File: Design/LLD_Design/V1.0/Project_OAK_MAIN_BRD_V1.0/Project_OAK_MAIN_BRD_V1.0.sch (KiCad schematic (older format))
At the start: 104 parts, among them U1 ATmega328PB-MU, U2 RV-8263-C7-32.768KHZ-20PPM-TA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, U3 LIS2DW12TR

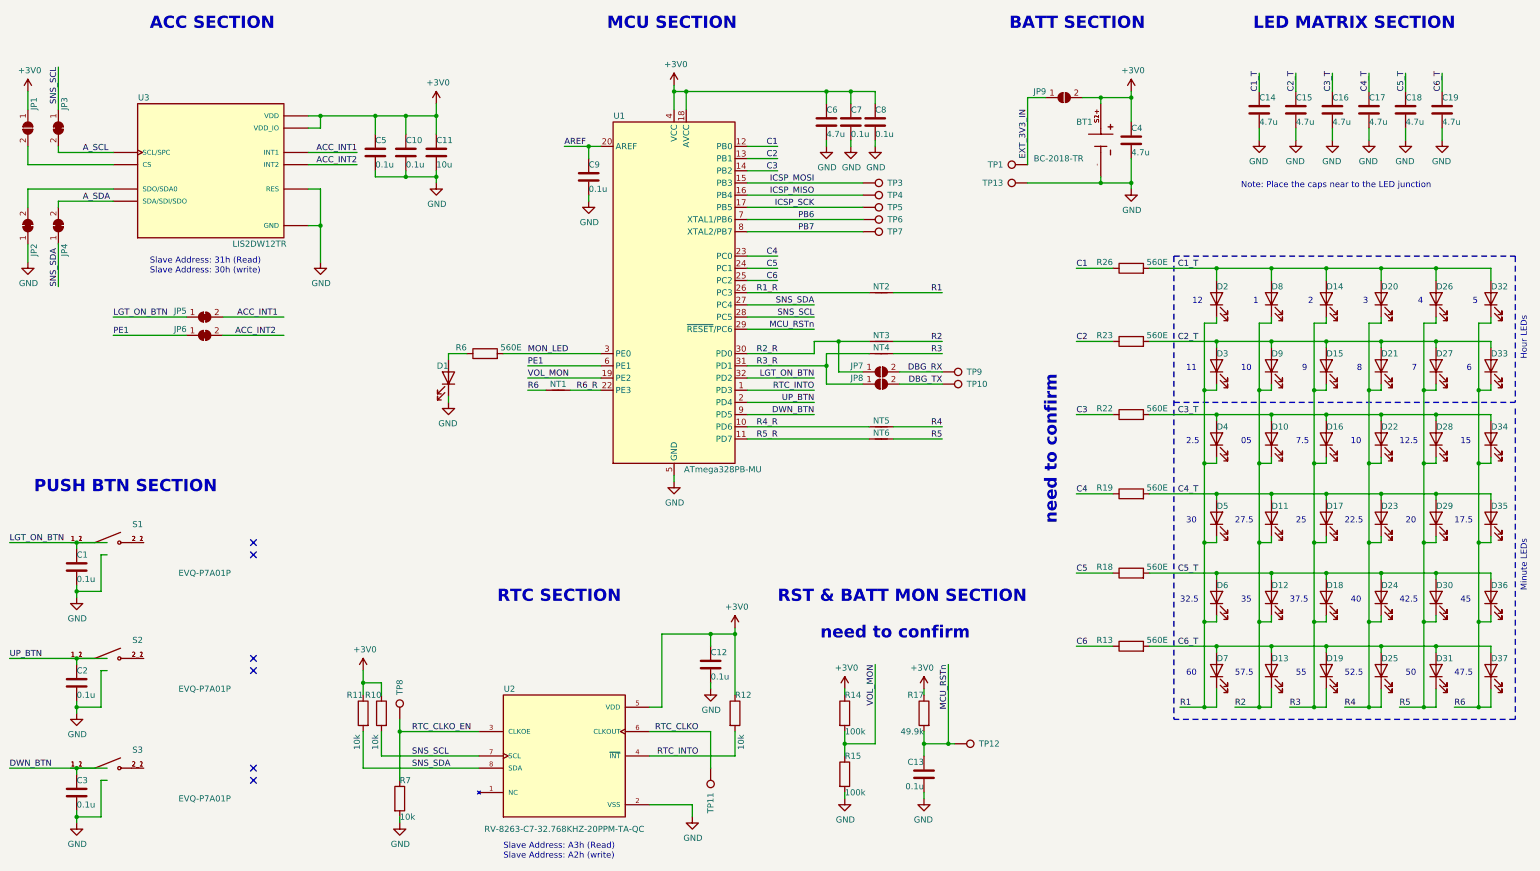
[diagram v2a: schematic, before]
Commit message: updated main board
changed main board stack up from 6L to 4L, updated schematics with symbol & footprint change for push button and updated main board outline with latest mechanical changes.
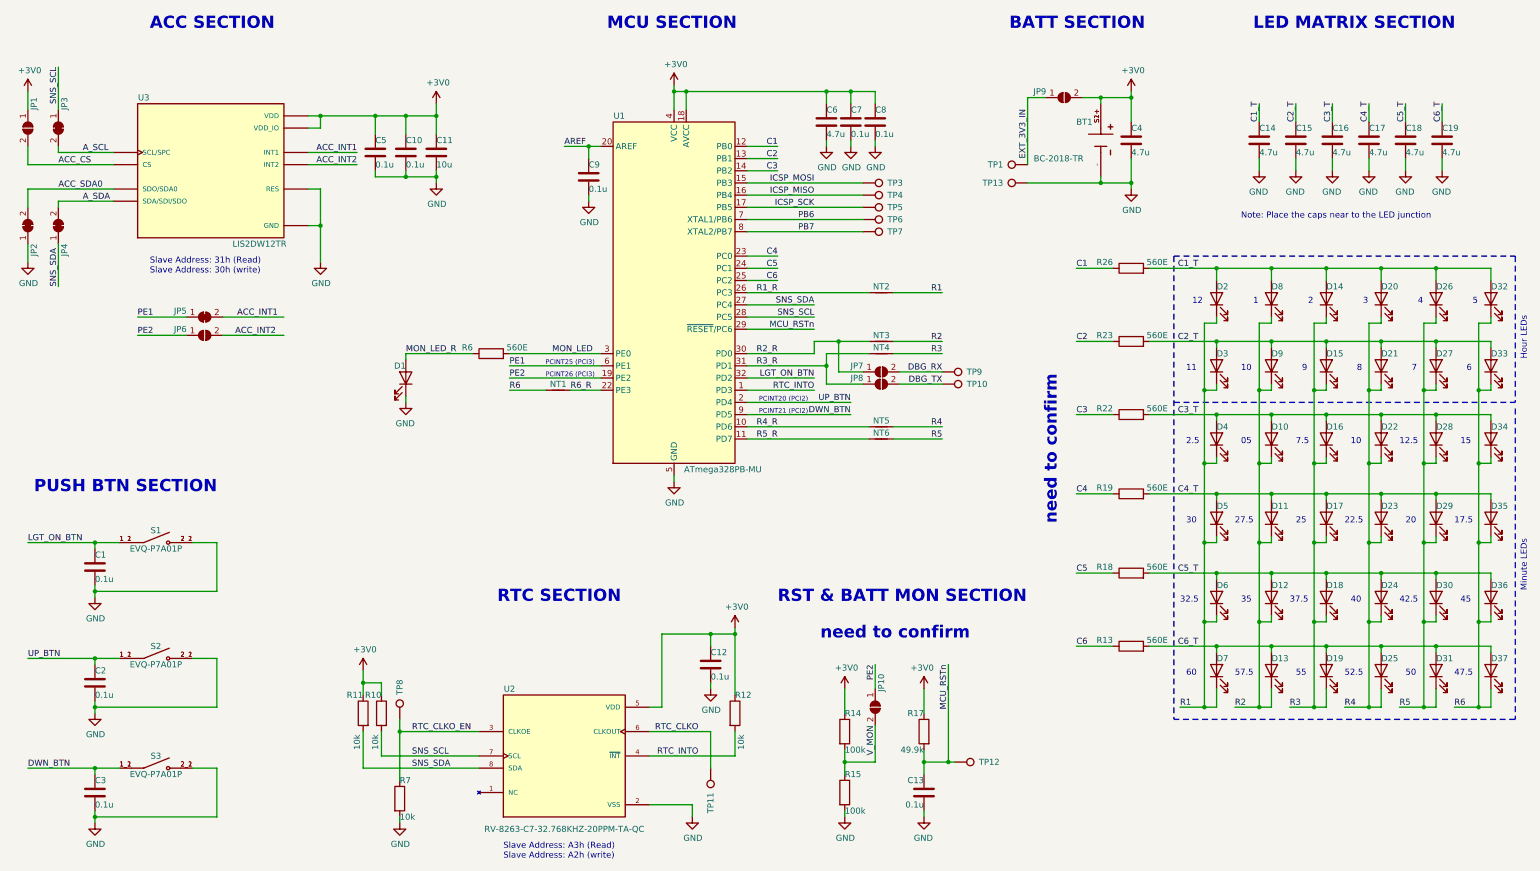
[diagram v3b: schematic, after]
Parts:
- removed JP6: SolderJumper_2_Bridged, Jumper:SolderJumper-2_P1.3mm_Bridged_RoundedPad1.0x1.5mm, symbol Jumper:SolderJumper_2_Bridged
- added JP10, JP6: SolderJumper_2_Open, Jumper:SolderJumper-2_P1.3mm_Open_RoundedPad1.0x1.5mm, symbol Jumper:SolderJumper_2_Open
- S1, S2, S3: footprint Button_Switch_SMD:EVQP7J01P -> Button_Switch_SMD:SW_EVQ-P7A01P
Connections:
- net labels added: ACC_CS, ACC_SDA0, MON_LED_R, PE2, V_MON
- net labels removed: VOL_MON
- wire segments 376 -> 377
- no-connect marks 6 -> 0
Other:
- note added: "PCINT20 (PCI2)"
- note added: "PCINT21 (PCI2)"
- note added: "PCINT25 (PCI3)"
- note added: "PCINT26 (PCI3)"
- moved on the sheet: C1, C13, C14, C15, C16, C17, C18, C19, C2, C3, D1, R14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

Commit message: Updated placement
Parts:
- removed JP3, JP4: SolderJumper_2_Bridged, Jumper:SolderJumper-2_P1.3mm_Bridged_RoundedPad1.0x1.5mm, symbol Jumper:SolderJumper_2_Bridged
- removed JP7, JP8: SolderJumper_2_Open, Jumper:SolderJumper-2_P1.3mm_Open_RoundedPad1.0x1.5mm, symbol Jumper:SolderJumper_2_Open
- removed TP10, TP8, TP9: TestPoint, TestPoint:TestPoint_Pad_D1.0mm, symbol Connector:TestPoint
- JP1, JP10, JP6, JP9: footprint Jumper:SolderJumper-2_P1.3mm_Open_RoundedPad1.0x1.5mm -> Jumper:SolderJumper-2_Open_Pad1.0x1.5mm_custom
- JP2, JP5: footprint Jumper:SolderJumper-2_P1.3mm_Bridged_RoundedPad1.0x1.5mm -> Jumper:SolderJumper-2_Bridged_Pad1.0x1.5mm_custom
- NT1, NT2, NT3, NT4, NT5, NT6: footprint NetTie:NetTie-2_SMD_Pad0.5mm -> NetTie:NetTie-2_SMD_Custom
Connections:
- net A_SCL is gone; now on net SNS_SCL: U3.1 (SCL/SPC)
- net A_SDA is gone; now on net SNS_SDA: U3.4 (SDA/SDI/SDO)
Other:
- moved on the sheet: NT3, NT4
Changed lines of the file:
@@
 Sheet 1 1
 Title "Project OAK MAIN BRD V1.0"
-Date "2025-09-21"
+Date "2025-10-20"
 Rev "A"
 Comp ""
@@
 Text Label 4200 6900 0    50   ~ 0
 SNS_SDA
-$Comp
-L Connector:TestPoint TP8
-U 1 1 6661317B
-P 4100 6500
-F 0 "TP8" V 4100 6700 50  0000 L CNN
-F 1 "TestPoint" H 4158 6527 50  0001 L CNN
-F 2 "TestPoint:TestPoint_Pad_D1.0mm" H 4300 6500 50  0001 C CNN
-F 3 "~" H 4300 6500 50  0001 C CNN
-	1    4100 6500
-	1    0    0    -1
-$EndComp
 Text Label 6550 6800 2    50   ~ 0
 RTC_INTO
@@
 Text Label 7500 3300 2    50   ~ 0
 MCU_RSTn
-Text Label 8550 3650 2    50   ~ 0
-DBG_RX
-Text Label 8550 3750 2    50   ~ 0
-DBG_TX
 Wire Wire Line
 	7500 3300 6950 3300
@@
 	1    9250 2100
 	0    -1   -1   0
-$EndComp
-$Comp
-L Connector:TestPoint TP10
-U 1 1 66909C2A
-P 8550 3750
-F 0 "TP10" V 8550 3950 50  0000 L CNN
-F 1 "TestPoint" H 8608 3777 50  0001 L CNN
-F 2 "TestPoint:TestPoint_Pad_D1.0mm" H 8750 3750 50  0001 C CNN
-F 3 "~" H 8750 3750 50  0001 C CNN
-	1    8550 3750
-	0    1    1    0
-$EndComp
-$Comp
-L Connector:TestPoint TP9
-U 1 1 66909C34
-P 8550 3650
-F 0 "TP9" V 8550 3850 50  0000 L CNN
-F 1 "TestPoint" H 8608 3677 50  0001 L CNN
-F 2 "TestPoint:TestPoint_Pad_D1.0mm" H 8750 3650 50  0001 C CNN
-F 3 "~" H 8750 3650 50  0001 C CNN
-	1    8550 3650
-	0    1    1    0
 $EndComp
 Text Label 6550 6600 2    50   ~ 0
@@
 Text Label 5500 3800 0    50   ~ 0
 R6_R
-Wire Wire Line
-	8200 3650 8550 3650
-Wire Wire Line
-	8200 3750 8550 3750
 Text Label 7200 4100 2    50   ~ 0
 R4_R
@@
 Text Label 8550 3000 2    50   ~ 0
 R1
-Text Label 8550 3400 2    50   ~ 0
+Text Label 8550 3500 2    50   ~ 0
 R2
-Text Label 8550 3500 2    50   ~ 0
+Text Label 8550 3600 2    50   ~ 0
 R3
 Wire Wire Line
-	8150 3400 8550 3400
-Wire Wire Line
 	8150 3500 8550 3500
 Wire Wire Line
-	7500 3500 7500 3400
-Wire Wire Line
-	7500 3400 7700 3400
-Wire Wire Line
-	6950 3500 7500 3500
-Wire Wire Line
-	7600 3600 7600 3500
-Wire Wire Line
-	7600 3500 7950 3500
-Wire Wire Line
-	6950 3600 7600 3600
-Wire Wire Line
-	7700 3400 7700 3650
-Connection ~ 7700 3400
-Wire Wire Line
-	7700 3400 7950 3400
-Wire Wire Line
-	7600 3600 7600 3750
-Connection ~ 7600 3600
+	8150 3600 8550 3600
 Text Notes 10600 3100 0    50   ~ 0
 12
@@
 Text Notes 10550 6150 0    50   ~ 0
 60
-Wire Wire Line
-	7700 3650 7900 3650
-Wire Wire Line
-	7600 3750 7900 3750
 $Comp
 L RV-8263-C7-32.768KHZ-20PPM-TA-QC:RV-8263-C7-32.768KHZ-20PPM-TA-QC U2
@@
 Text Label 5000 3600 0    50   ~ 0
 PE1
-Wire Wire Line
-	4100 6500 4100 6600
 $Comp
 L Device:R R7
@@
 Wire Wire Line
 	4100 7000 4100 6600
-Connection ~ 4100 6600
 Wire Wire Line
 	1600 5400 1600 5450
@@
 Wire Wire Line
 	3450 1550 3900 1550
-Wire Wire Line
-	1300 2950 1300 2600
-$Comp
-L Jumper:SolderJumper_2_Bridged JP4
-U 1 1 693258B0
-P 1300 2450
-F 0 "JP4" H 1100 2500 50  0000 C CNN
-F 1 "SolderJumper_2_Bridged" H 1300 2564 50  0001 C CNN
-F 2 "Jumper:SolderJumper-2_P1.3mm_Bridged_RoundedPad1.0x1.5mm" H 1300 2450 50  0001 C CNN
-F 3 "~" H 1300 2450 50  0001 C CNN
-	1    1300 2450
-	0    1    -1   0
-$EndComp
-$Comp
-L Jumper:SolderJumper_2_Bridged JP3
-U 1 1 6939B47C
-P 1300 1650
-F 0 "JP3" H 1100 1700 50  0000 C CNN
-F 1 "SolderJumper_2_Bridged" H 1300 1764 50  0001 C CNN
-F 2 "Jumper:SolderJumper-2_P1.3mm_Bridged_RoundedPad1.0x1.5mm" H 1300 1650 50  0001 C CNN
-F 3 "~" H 1300 1650 50  0001 C CNN
-	1    1300 1650
-	0    1    1    0
-$EndComp
-Text Label 1500 2250 0    50   ~ 0
-A_SDA
-Text Label 1500 1850 0    50   ~ 0
-A_SCL
 $Comp
 L power:GND #PWR03
@@
 Wire Wire Line
 	1050 1950 1750 1950
-Wire Wire Line
-	1300 1150 1300 1500
 Text Label 1300 1150 3    50   ~ 0
 SNS_SCL
@@
 SNS_SDA
 Wire Wire Line
-	1300 1800 1300 1850
-Wire Wire Line
 	1300 1850 1750 1850
-Wire Wire Line
-	1300 2300 1300 2250
 Wire Wire Line
 	1300 2250 1750 2250
@@
 F 0 "JP5" H 2300 3250 50  0000 C CNN
 F 1 "SolderJumper_2_Bridged" H 2500 3314 50  0001 C CNN
-F 2 "Jumper:SolderJumper-2_P1.3mm_Bridged_RoundedPad1.0x1.5mm" H 2500 3200 50  0001 C CNN
+F 2 "Jumper:SolderJumper-2_Bridged_Pad1.0x1.5mm_custom" H 2500 3200 50  0001 C CNN
 F 3 "~" H 2500 3200 50  0001 C CNN
 	1    2500 3200
@@
 F 0 "JP2" H 850 2500 50  0000 C CNN
 F 1 "SolderJumper_2_Bridged" H 1050 2564 50  0001 C CNN
-F 2 "Jumper:SolderJumper-2_P1.3mm_Bridged_RoundedPad1.0x1.5mm" H 1050 2450 50  0001 C CNN
+F 2 "Jumper:SolderJumper-2_Bridged_Pad1.0x1.5mm_custom" H 1050 2450 50  0001 C CNN
 F 3 "~" H 1050 2450 50  0001 C CNN
 	1    1050 2450
@@
 F 0 "JP1" H 850 1700 50  0000 C CNN
 F 1 "SolderJumper_2_Open" H 1050 1764 50  0001 C CNN
-F 2 "Jumper:SolderJumper-2_P1.3mm_Open_RoundedPad1.0x1.5mm" H 1050 1650 50  0001 C CNN
+F 2 "Jumper:SolderJumper-2_Open_Pad1.0x1.5mm_custom" H 1050 1650 50  0001 C CNN
 F 3 "~" H 1050 1650 50  0001 C CNN
 	1    1050 1650
 	0    1    1    0
-$EndComp
-$Comp
-L Jumper:SolderJumper_2_Open JP7
-U 1 1 6A97A748
-P 8050 3650
-F 0 "JP7" H 7850 3700 50  0000 C CNN
-F 1 "SolderJumper_2_Open" H 8050 3764 50  0001 C CNN
-F 2 "Jumper:SolderJumper-2_P1.3mm_Open_RoundedPad1.0x1.5mm" H 8050 3650 50  0001 C CNN
-F 3 "~" H 8050 3650 50  0001 C CNN
-	1    8050 3650
-	1    0    0    -1
-$EndComp
-$Comp
-L Jumper:SolderJumper_2_Open JP8
-U 1 1 6A9CEA05
-P 8050 3750
-F 0 "JP8" H 7850 3800 50  0000 C CNN
-F 1 "SolderJumper_2_Open" H 8050 3864 50  0001 C CNN
-F 2 "Jumper:SolderJumper-2_P1.3mm_Open_RoundedPad1.0x1.5mm" H 8050 3750 50  0001 C CNN
-F 3 "~" H 8050 3750 50  0001 C CNN
-	1    8050 3750
-	1    0    0    -1
 $EndComp
 $Comp
@@
 F 0 "NT2" H 8050 3050 50  0000 C CNN
 F 1 "Net-Tie_2" H 8050 3090 50  0001 C CNN
-F 2 "NetTie:NetTie-2_SMD_Pad0.5mm" H 8050 3000 50  0001 C CNN
+F 2 "NetTie:NetTie-2_SMD_Custom" H 8050 3000 50  0001 C CNN
 F 3 "~" H 8050 3000 50  0001 C CNN
 	1    8050 3000
@@
 L Device:Net-Tie_2 NT3
 U 1 1 6AAA1105
-P 8050 3400
-F 0 "NT3" H 8050 3450 50  0000 C CNN
-F 1 "Net-Tie_2" H 8050 3490 50  0001 C CNN
-F 2 "NetTie:NetTie-2_SMD_Pad0.5mm" H 8050 3400 50  0001 C CNN
-F 3 "~" H 8050 3400 50  0001 C CNN
-	1    8050 3400
+P 8050 3500
+F 0 "NT3" H 8050 3550 50  0000 C CNN
+F 1 "Net-Tie_2" H 8050 3590 50  0001 C CNN
+F 2 "NetTie:NetTie-2_SMD_Custom" H 8050 3500 50  0001 C CNN
+F 3 "~" H 8050 3500 50  0001 C CNN
+	1    8050 3500
 	1    0    0    -1
 $EndComp
@@
 L Device:Net-Tie_2 NT4
 U 1 1 6AAC9C1E
-P 8050 3500
-F 0 "NT4" H 8050 3550 50  0000 C CNN
-F 1 "Net-Tie_2" H 8050 3590 50  0001 C CNN
-F 2 "NetTie:NetTie-2_SMD_Pad0.5mm" H 8050 3500 50  0001 C CNN
-F 3 "~" H 8050 3500 50  0001 C CNN
-	1    8050 3500
+P 8050 3600
+F 0 "NT4" H 8050 3650 50  0000 C CNN
+F 1 "Net-Tie_2" H 8050 3690 50  0001 C CNN
+F 2 "NetTie:NetTie-2_SMD_Custom" H 8050 3600 50  0001 C CNN
+F 3 "~" H 8050 3600 50  0001 C CNN
+	1    8050 3600
 	1    0    0    -1
 $EndComp
@@
 F 0 "NT5" H 8050 4150 50  0000 C CNN
 F 1 "Net-Tie_2" H 8050 4190 50  0001 C CNN
-F 2 "NetTie:NetTie-2_SMD_Pad0.5mm" H 8050 4100 50  0001 C CNN
+F 2 "NetTie:NetTie-2_SMD_Custom" H 8050 4100 50  0001 C CNN
 F 3 "~" H 8050 4100 50  0001 C CNN
 	1    8050 4100
@@
 F 0 "NT6" H 8050 4250 50  0000 C CNN
 F 1 "Net-Tie_2" H 8050 4290 50  0001 C CNN
-F 2 "NetTie:NetTie-2_SMD_Pad0.5mm" H 8050 4200 50  0001 C CNN
+F 2 "NetTie:NetTie-2_SMD_Custom" H 8050 4200 50  0001 C CNN
 F 3 "~" H 8050 4200 50  0001 C CNN
 	1    8050 4200
@@
 F 0 "NT1" H 5400 3850 50  0000 C CNN
 F 1 "Net-Tie_2" H 5400 3890 50  0001 C CNN
-F 2 "NetTie:NetTie-2_SMD_Pad0.5mm" H 5400 3800 50  0001 C CNN
+F 2 "NetTie:NetTie-2_SMD_Custom" H 5400 3800 50  0001 C CNN
 F 3 "~" H 5400 3800 50  0001 C CNN
 	1    5400 3800
@@
 F 0 "JP9" H 9350 1450 50  0000 C CNN
 F 1 "SolderJumper_2_Open" H 9550 1514 50  0001 C CNN
-F 2 "Jumper:SolderJumper-2_P1.3mm_Open_RoundedPad1.0x1.5mm" H 9550 1400 50  0001 C CNN
+F 2 "Jumper:SolderJumper-2_Open_Pad1.0x1.5mm_custom" H 9550 1400 50  0001 C CNN
 F 3 "~" H 9550 1400 50  0001 C CNN
 	1    9550 1400
@@
 F 0 "JP6" H 2300 3400 50  0000 C CNN
 F 1 "SolderJumper_2_Open" H 2500 3464 50  0001 C CNN
-F 2 "Jumper:SolderJumper-2_P1.3mm_Open_RoundedPad1.0x1.5mm" H 2500 3350 50  0001 C CNN
+F 2 "Jumper:SolderJumper-2_Open_Pad1.0x1.5mm_custom" H 2500 3350 50  0001 C CNN
 F 3 "~" H 2500 3350 50  0001 C CNN
 	1    2500 3350
@@
 F 0 "JP10" H 7800 6450 50  0000 C CNN
 F 1 "SolderJumper_2_Open" H 8000 6514 50  0001 C CNN
-F 2 "Jumper:SolderJumper-2_P1.3mm_Open_RoundedPad1.0x1.5mm" H 8000 6400 50  0001 C CNN
+F 2 "Jumper:SolderJumper-2_Open_Pad1.0x1.5mm_custom" H 8000 6400 50  0001 C CNN
 F 3 "~" H 8000 6400 50  0001 C CNN
 	1    8000 6400
@@
 	0    -1   -1   0
 $EndComp
+Wire Wire Line
+	1300 1150 1300 1850
+Wire Wire Line
+	1300 2250 1300 2950
+Wire Wire Line
+	6950 3600 7950 3600
+Wire Wire Line
+	6950 3500 7950 3500
 $EndSCHEMATC
